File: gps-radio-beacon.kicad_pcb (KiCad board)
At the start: 2 copper layers, 106.4 x 69.7 mm, 34 parts, among them J1 Conn_01x16, J2 Conn_01x16, J3 Conn_Coaxial, J4 Conn_Coaxial, P1 USB_C_Plug_USB2.0, Q1 Q_PMOS_DGS, U1 PGA2040, U2 Si4463, U3 MAX-M10S, U4 NCP1117-3.3_SOT223

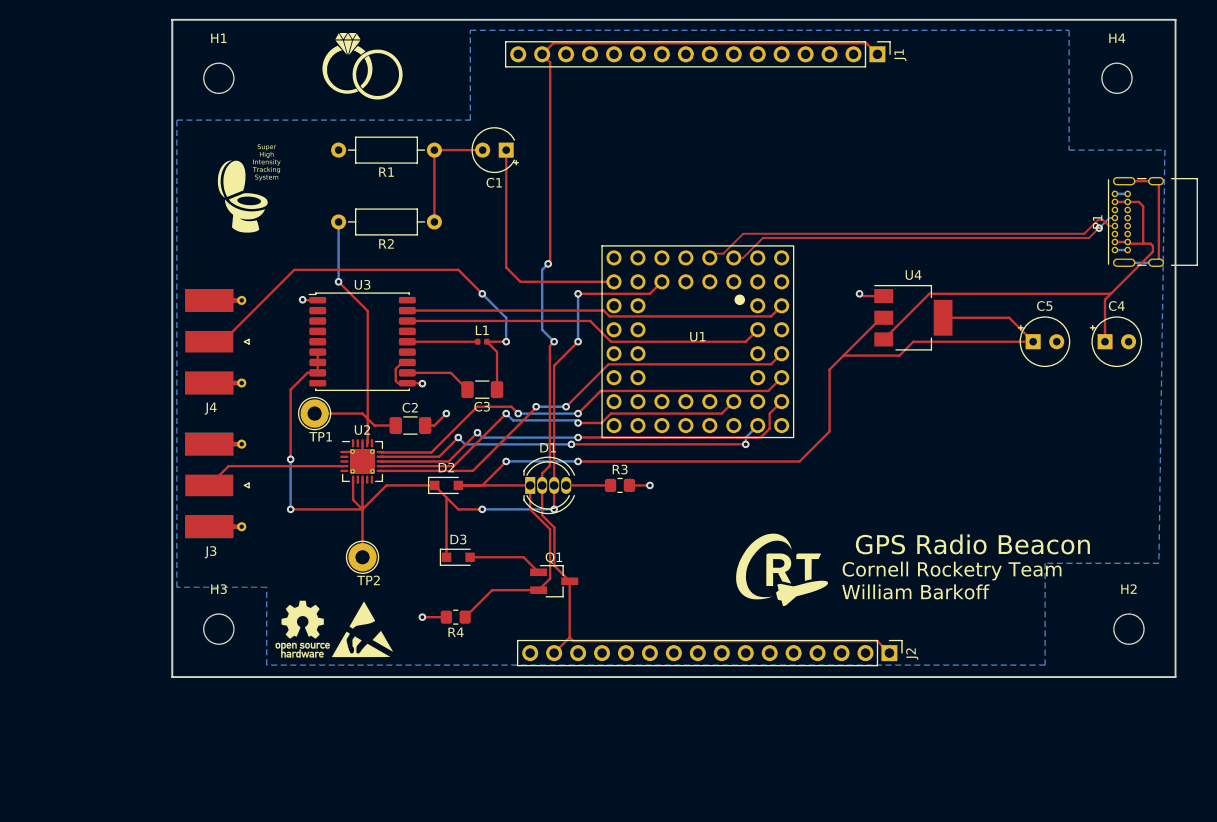
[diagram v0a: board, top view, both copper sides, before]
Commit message: redesign for use with RFM95
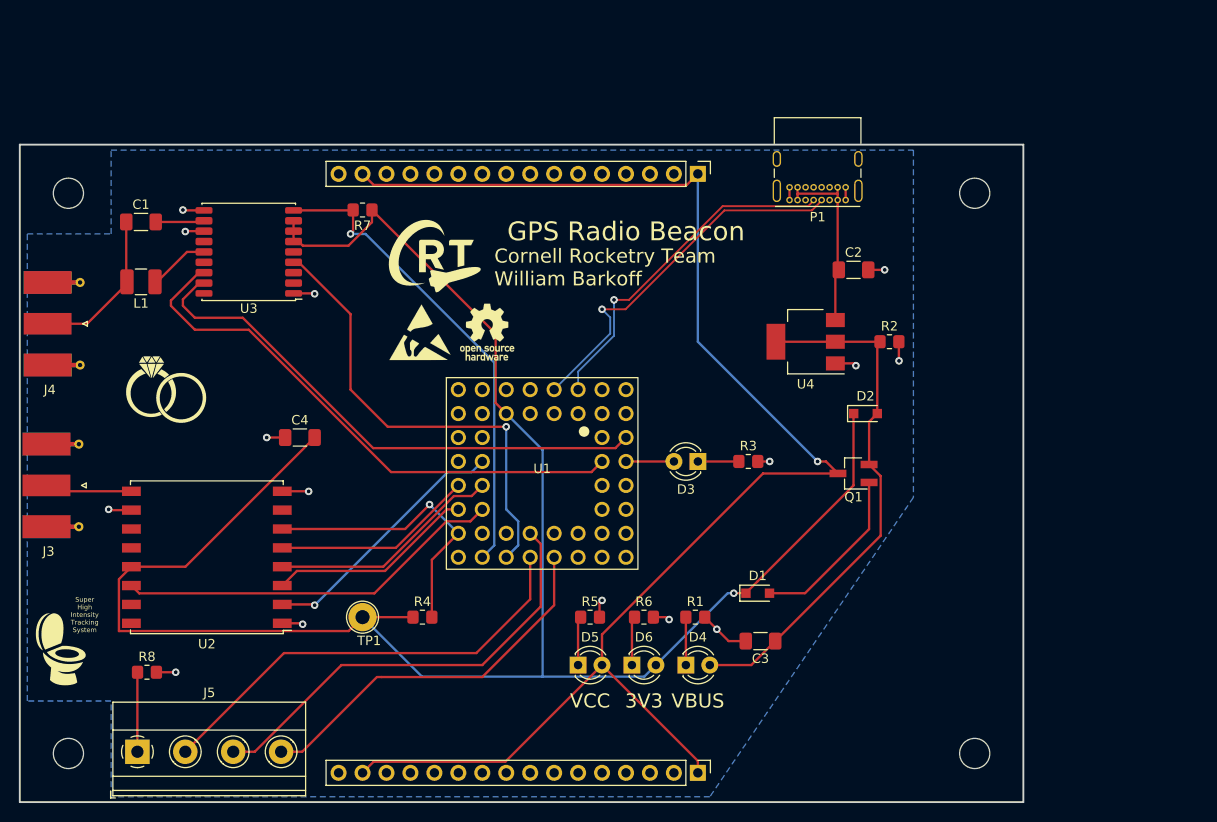
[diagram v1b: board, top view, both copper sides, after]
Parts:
- removed C5: 10u, Capacitor_THT:CP_Radial_Tantal_D5.0mm_P2.50mm
- removed TP2: TestPoint, TestPoint:TestPoint_Loop_D2.54mm_Drill1.5mm_Beaded
- added D4: LED, LED_THT:LED_D3.0mm, F.Cu at (153.7, 130.8)
- added D5: LED, LED_THT:LED_D3.0mm, F.Cu at (142.2, 130.8)
- added D6: LED, LED_THT:LED_D3.0mm, F.Cu at (147.9, 130.8)
- added J5: Screw_Terminal_01x04, TerminalBlock_Phoenix:TerminalBlock_Phoenix_MKDS-1,5-4-5.08_1x04_P5.08mm_Horizontal, F.Cu at (95.5, 140.0)
- added R5: 200, Resistor_SMD:R_0805_2012Metric_Pad1.20x1.40mm_HandSolder, F.Cu at (143.5, 125.7)
- added R6: 200, Resistor_SMD:R_0805_2012Metric_Pad1.20x1.40mm_HandSolder, F.Cu at (149.2, 125.7)
- added R7: 10k, Resistor_SMD:R_0805_2012Metric_Pad1.20x1.40mm_HandSolder, F.Cu at (119.4, 82.5)
- added R8: 200, Resistor_SMD:R_0805_2012Metric_Pad1.20x1.40mm_HandSolder, F.Cu at (96.5, 131.6)
- C1: value 100n -> 10n; footprint Capacitor_THT:CP_Radial_Tantal_D4.5mm_P2.50mm -> Capacitor_SMD:C_1206_3216Metric_Pad1.33x1.80mm_HandSolder
- C2: value 4.7n -> 10u
- C3: value 10n -> 10u
- C4: footprint Capacitor_THT:CP_Radial_Tantal_D5.0mm_P2.50mm -> Capacitor_SMD:C_1206_3216Metric_Pad1.33x1.80mm_HandSolder
- D1: value LED_RGBK -> D_Schottky; footprint LED_THT:LED_D5.0mm-4_RGB -> Diode_SMD:D_SOD-323_HandSoldering
- D3: value D_Schottky -> LED; footprint Diode_SMD:D_SOD-323_HandSoldering -> LED_THT:LED_D3.0mm
- L1: footprint Inductor_SMD:L_0402_1005Metric -> Inductor_SMD:L_1210_3225Metric_Pad1.42x2.65mm_HandSolder
- R1: value 4.7k -> 200; footprint Resistor_THT:R_Axial_DIN0207_L6.3mm_D2.5mm_P10.16mm_Horizontal -> Resistor_SMD:R_0805_2012Metric_Pad1.20x1.40mm_HandSolder
- R2: value 4.7k -> 10k; footprint Resistor_THT:R_Axial_DIN0207_L6.3mm_D2.5mm_P10.16mm_Horizontal -> Resistor_SMD:R_0805_2012Metric_Pad1.20x1.40mm_HandSolder
- U2: value Si4463 -> RFM95W-915S2; footprint Package_DFN_QFN:QFN-20-1EP_4x4mm_P0.5mm_EP2.6x2.6mm_ThermalVias -> RF_Module:HOPERF_RFM9XW_SMD
- moved C4 86.0 mm to (112.7, 106.7)
- moved H4 73.2 mm to (184.3, 140.2)
- moved R1 56.7 mm to (154.7, 125.7), turned to 0 degrees
- moved G*** 51.7 mm to (87.4, 129.3)
- moved R2 49.9 mm to (175.3, 96.5), turned to 0 degrees
- moved C2 49.8 mm to (171.4, 88.9)
- moved G*** 49.6 mm to (127.0, 87.4)
- moved H2 49.0 mm to (184.3, 80.8)
- moved D2 45.1 mm to (172.7, 104.1)
- moved G*** 40.1 mm to (98.6, 101.6)
- moved C3 39.8 mm to (161.6, 128.3)
- moved C1 39.5 mm to (95.9, 83.8), turned to 0 degrees
- moved REF** 37.1 mm to (132.6, 95.5)
- moved L1 36.7 mm to (95.9, 90.2), turned to 180 degrees
- moved Q1 33.7 mm to (171.4, 110.5), turned to 180 degrees
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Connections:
- C2 pad 1: /AFSK_SIGNAL -> +5V
- C2 pad 2: GND -> <NO NET>
- C3 pad 1: Net-(C3-Pad1) -> VBUS
- C3 pad 2: Net-(C3-Pad2) -> <NO NET>
- C4 pad 1: Net-(C4-Pad1) -> <NO NET>
- C4 pad 2: GND -> +3V3
- D1 pad 1: VBUS -> +3V3
- D1 pad 2: VCC -> Net-(D1-Pad2)
- D3 pad 1: +3V3 -> Net-(D3-Pad1)
- J1 pad 16: GND -> <NO NET>
- J1 pad 2: GND -> <NO NET>
- J2 pad 16: GND -> <NO NET>
- J2 pad 2: GND -> <NO NET>
- J3 pad 2: GND -> <NO NET>
- J4 pad 1: Net-(C3-Pad1) -> Net-(C1-Pad1)
- J4 pad 2: GND -> <NO NET>
- L1 pad 2: Net-(C3-Pad1) -> Net-(C1-Pad1)
- P1 pad A1: GND -> <NO NET>
- P1 pad A12: GND -> <NO NET>
- P1 pad A4: Net-(C4-Pad1) -> +5V
- P1 pad A9: Net-(C4-Pad1) -> +5V
- P1 pad B1: GND -> <NO NET>
- P1 pad B12: GND -> <NO NET>
- P1 pad B4: Net-(C4-Pad1) -> +5V
- P1 pad B9: Net-(C4-Pad1) -> +5V
- P1 pad S1: unconnected-(P1-PadS1) -> <NO NET>
- Q1 pad 1: Net-(D3-Pad2) -> Net-(D1-Pad2)
- R1 pad 1: Net-(C1-Pad2) -> Net-(D4-Pad1)
- R1 pad 2: GND -> <NO NET>
- R2 pad 1: Net-(C1-Pad2) -> VBUS
- R2 pad 2: /AFSK_SIGNAL -> <NO NET>
- R3 pad 1: Net-(D1-Pad4) -> Net-(D3-Pad1)
- R3 pad 2: GND -> <NO NET>
- R4 pad 1: VBUS -> +3V3
- R4 pad 2: GND -> /RADIO_RESET
- TP1 pad 1: /AFSK_SIGNAL -> +3V3
- U1 pad A1: GND -> <NO NET>
- U1 pad A3: GND -> <NO NET>
- U1 pad A8: GND -> <NO NET>
- U1 pad B1: Net-(C1-Pad1) -> unconnected-(U1-PadB1)
- U1 pad B2: GND -> <NO NET>
- U1 pad B7: GND -> <NO NET>
- U1 pad D2: unconnected-(U1-PadD2) -> /RADIO_MISO
- U1 pad D8: unconnected-(U1-PadD8) -> Net-(D3-Pad2)
- U1 pad E1: unconnected-(U1-PadE1) -> /RADIO_CS
- U1 pad E2: unconnected-(U1-PadE2) -> /RADIO_SCK
- U1 pad E8: /~{RADIO_INT} -> unconnected-(U1-PadE8)
- U1 pad F1: unconnected-(U1-PadF1) -> /RADIO_MOSI
- U1 pad F2: unconnected-(U1-PadF2) -> /RADIO_IRQ
- U1 pad F8: /~{RADIO_CS} -> unconnected-(U1-PadF8)
- U1 pad G1: unconnected-(U1-PadG1) -> /RADIO_RESET
- U1 pad G2: GND -> <NO NET>
- U1 pad G4: unconnected-(U1-PadG4) -> /IND_LED_2
- U1 pad G6: /RADIO_SCLK -> unconnected-(U1-PadG6)
- U1 pad G7: GND -> <NO NET>
- U1 pad G8: /RADIO_MISO -> unconnected-(U1-PadG8)
- U1 pad H1: GND -> <NO NET>
- U1 pad H2: unconnected-(U1-PadH2) -> /GPS_RESET
- U1 pad H3: unconnected-(U1-PadH3) -> /GPS_TIMEPULSE
- U1 pad H4: unconnected-(U1-PadH4) -> /IND_LED_1
- U1 pad H5: unconnected-(U1-PadH5) -> /IND_LED_3
- U1 pad H7: /RADIO_MOSI -> unconnected-(U1-PadH7)
- U1 pad H8: GND -> <NO NET>
- U2 pad 1: GND -> <NO NET>
- U2 pad 10: unconnected-(U2-Pad10) -> <NO NET>
- U2 pad 11: /~{RADIO_INT} -> unconnected-(U2-Pad11)
- U2 pad 12: /RADIO_SCLK -> unconnected-(U2-Pad12)
- U2 pad 13: /RADIO_MISO -> +3V3
- U2 pad 14: /RADIO_MOSI -> /RADIO_IRQ
- U2 pad 15: /~{RADIO_CS} -> unconnected-(U2-Pad15)
- U2 pad 2: unconnected-(U2-Pad2) -> /RADIO_MISO
- U2 pad 3: unconnected-(U2-Pad3) -> /RADIO_MOSI
- U2 pad 4: Net-(J3-Pad1) -> /RADIO_SCK
- U2 pad 5: unconnected-(U2-Pad5) -> /RADIO_CS
- U2 pad 6: +3V3 -> /RADIO_RESET
- U2 pad 8: +3V3 -> <NO NET>
- U2 pad 9: unconnected-(U2-Pad9) -> Net-(J3-Pad1)
- U3 pad 1: GND -> <NO NET>
- U3 pad 10: GND -> <NO NET>
- U3 pad 11: Net-(C3-Pad2) -> Net-(C1-Pad2)
- U3 pad 12: GND -> <NO NET>
- U3 pad 9: unconnected-(U3-Pad9) -> /GPS_RESET
- U4 pad 1: GND -> <NO NET>
- U4 pad 3: Net-(C4-Pad1) -> +5V
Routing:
- net +3V3: track 100.1 -> 205.0 mm, vias 6 -> 1
- net VBUS: track 116.5 -> 56.4 mm, vias 2 -> 0
- net /GPS_RESET: track 0.00 -> 51.0 mm, vias 0 -> 1
- net Net-(C4-Pad1): track 49.6 -> 0.00 mm
- net /GPS_TIMEPULSE: track 0.00 -> 49.4 mm, vias 0 -> 1
- net /~{RADIO_INT}: track 47.9 -> 0.00 mm, vias 2 -> 0
- net /IND_LED_1: track 0.00 -> 47.7 mm
- net /IND_LED_2: track 0.00 -> 47.2 mm
- net /~{RADIO_CS}: track 46.4 -> 0.00 mm, vias 2 -> 0
- net Net-(C3-Pad1): track 45.5 -> 0.00 mm, vias 2 -> 0
- net /RADIO_IRQ: track 0.00 -> 41.2 mm
- net /RADIO_SCLK: track 41.1 -> 0.00 mm, vias 2 -> 0
- net /IND_LED_3: track 0.00 -> 40.4 mm
- net <NO NET>: track 0.00 -> 37.1 mm, vias 0 -> 15
- net /AFSK_SIGNAL: track 32.6 -> 0.00 mm, vias 1 -> 0
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- added copper zone on B.Cu, net <NO NET>
- removed copper zone on B.Cu, net GND
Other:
- board text added: "3V3"
- board text added: "REV YYYY-MM-DD"
- board text added: "VBUS"
- board text added: "VCC"
- board text removed: "REV 2022-11-20"

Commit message: rearrange a few components
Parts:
- removed the G*** at (98.6, 101.6)
- moved G*** 52.6 mm to (166.6, 121.9)
- moved REF** 51.7 mm to (183.9, 88.9)
- moved G*** 46.3 mm to (98.6, 84.3)
- moved REF** 25.2 mm to (102.6, 106.2)
- moved C3 24.3 mm to (178.3, 110.7), turned to 0 degrees
- moved C4 24.2 mm to (114.3, 130.8)
- moved L1 10.8 mm to (95.2, 101.0)
- moved R7 10.8 mm to (118.7, 93.3)
- moved U3 10.8 mm to (106.7, 97.8)
- moved C1 10.8 mm to (96.0, 94.6)
- moved R1 8.39 mm to (146.3, 126.0)
- moved D4 8.38 mm to (145.3, 130.8)
- moved D6 8.00 mm to (139.9, 130.8)
- moved R6 7.99 mm to (141.2, 126.0)
- moved R5 7.89 mm to (135.6, 126.0)
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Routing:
- net +3V3: track 205.0 -> 169.7 mm
- net VCC: track 156.1 -> 170.6 mm, vias 1 -> 2
- net /GPS_TIMEPULSE: track 49.4 -> 40.8 mm
- net VBUS: track 56.4 -> 64.2 mm
- net /GPS_RESET: track 51.0 -> 47.4 mm
- net <NO NET>: track 37.1 -> 39.5 mm, vias 15 -> 16
- net Net-(D1-Pad2): track 18.3 -> 20.0 mm
- net /IND_LED_3: track 40.4 -> 39.0 mm
- net /IND_LED_2: track 47.2 -> 45.9 mm
- net Net-(C1-Pad1): track 16.9 -> 15.6 mm
- net /GPS_SCL: track 57.3 -> 56.0 mm
- net /IND_LED_1: track 47.7 -> 46.6 mm
- net Net-(C1-Pad2): track 5.17 -> 4.41 mm
- net /GPS_SDA: track 58.8 -> 59.4 mm
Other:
- board text added: "Alpha"
- board text added: "Beta"
- board text added: "GPS"
- board text added: "GPS Radio Beacon Cornell Rocketry William Barkoff Nov 28, 2022"
- board text added: "RF"
- board text removed: "Cornell Rocketry Team William Barkoff"
- board text removed: "GPS Radio Beacon"

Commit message: reroute some stuff
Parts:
- moved R7 1.81 mm to (117.3, 94.5), turned to 90 degrees
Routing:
- net +3V3: track 169.7 -> 166.5 mm
- net /GPS_RESET: track 47.4 -> 46.2 mm
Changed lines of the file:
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@@
   )
   (footprint "Resistor_SMD:R_0805_2012Metric_Pad1.20x1.40mm_HandSolder" (layer "F.Cu")
-    (at 118.745 93.345 180)
+    (at 117.348 94.488 90)
     (descr "Resistor SMD 0805 (2012 Metric), square (rectangular) end terminal, IPC_7351 nominal with elongated pad for handsoldering. (Body size source: IPC-SM-782 page 72, https://www.pcb-3d.com/wordpress/wp-content/uploads/ipc-sm-782a_amendment_1_and_2.pdf), generated with kicad-footprint-generator")
     (tags "resistor handsolder")
@@
     (property "Sheetname" "")
     (attr smd)
-    (fp_text reference "R7" (at 0 -1.65) (layer "F.SilkS")
+    (fp_text reference "R7" (at 2.54 0 180) (layer "F.SilkS")
       (effects (font (size 1 1) (thickness 0.15)))
     )
-    (fp_text value "10k" (at 0 1.65) (layer "F.Fab")
+    (fp_text value "10k" (at 0 1.65 90) (layer "F.Fab")
       (effects (font (size 1 1) (thickness 0.15)))
     )
-    (fp_text user "${REFERENCE}" (at 0 0) (layer "F.Fab")
+    (fp_text user "${REFERENCE}" (at 0 0 90) (layer "F.Fab")
       (effects (font (size 0.5 0.5) (thickness 0.08)))
     )
@@
     (fp_line (start 1 -0.625) (end 1 0.625) (layer "F.Fab") (width 0.1))
     (fp_line (start -1 -0.625) (end 1 -0.625) (layer "F.Fab") (width 0.1))
-    (pad "1" smd roundrect (at -1 0 180) (size 1.2 1.4) (layers "F.Cu" "F.Paste" "F.Mask") (roundrect_rratio 0.208333)
+    (pad "1" smd roundrect (at -1 0 90) (size 1.2 1.4) (layers "F.Cu" "F.Paste" "F.Mask") (roundrect_rratio 0.208333)
       (net 5 "+3V3") (pintype "passive"))
-    (pad "2" smd roundrect (at 1 0 180) (size 1.2 1.4) (layers "F.Cu" "F.Paste" "F.Mask") (roundrect_rratio 0.208333)
+    (pad "2" smd roundrect (at 1 0 90) (size 1.2 1.4) (layers "F.Cu" "F.Paste" "F.Mask") (roundrect_rratio 0.208333)
       (net 48 "/GPS_RESET") (pintype "passive"))
     (model "${KICAD6_3DMODEL_DIR}/Resistor_SMD.3dshapes/R_0805_2012Metric.wrl"
@@
   (segment (start 117.251536 97.133769) (end 112.416231 97.133769) (width 0.25) (layer "F.Cu") (net 5))
   (segment (start 115.775 130.7225) (end 115.775 127.205) (width 0.25) (layer "F.Cu") (net 5))
+  (segment (start 117.348 95.488) (end 117.348 97.037305) (width 0.25) (layer "F.Cu") (net 5))
   (segment (start 119.38 125.73) (end 124.73 125.73) (width 0.25) (layer "F.Cu") (net 5))
   (segment (start 111.43 95.59) (end 111.43 94.49) (width 0.25) (layer "F.Cu") (net 5))
@@
   (segment (start 143.764 124.968) (end 143.764 129.535) (width 0.25) (layer "F.Cu") (net 5))
   (segment (start 154.8384 118.872) (end 153.69 118.872) (width 0.25) (layer "F.Cu") (net 5))
+  (segment (start 117.348 97.037305) (end 117.251536 97.133769) (width 0.25) (layer "F.Cu") (net 5))
   (segment (start 115.775 127.205) (end 117.905 127.205) (width 0.25) (layer "F.Cu") (net 5))
-  (segment (start 119.745 94.640305) (end 117.251536 97.133769) (width 0.25) (layer "F.Cu") (net 5))
   (segment (start 117.905 127.205) (end 119.38 125.73) (width 0.25) (layer "F.Cu") (net 5))
   (segment (start 93.545 127.205) (end 115.775 127.205) (width 0.25) (layer "F.Cu") (net 5))
@@
   (segment (start 115.8625 130.81) (end 115.775 130.7225) (width 0.25) (layer "F.Cu") (net 5))
   (segment (start 93.545 121.705) (end 93.545 127.205) (width 0.25) (layer "F.Cu") (net 5))
-  (segment (start 119.745 93.345) (end 119.745 94.640305) (width 0.25) (layer "F.Cu") (net 5))
   (segment (start 149.86 118.872) (end 143.764 124.968) (width 0.25) (layer "F.Cu") (net 5))
   (segment (start 111.972462 96.69) (end 111.43 96.69) (width 0.25) (layer "F.Cu") (net 5))
@@
   (via (at 126.4877 113.7877) (size 0.8) (drill 0.4) (layers "F.Cu" "B.Cu") (net 47))
   (segment (start 126.4877 113.7877) (end 129.54 116.84) (width 0.25) (layer "B.Cu") (net 47))
-  (segment (start 114.89 93.39) (end 117.7 93.39) (width 0.25) (layer "F.Cu") (net 48))
-  (segment (start 111.43 93.39) (end 114.89 93.39) (width 0.25) (layer "F.Cu") (net 48))
-  (segment (start 117.348 93.742) (end 117.745 93.345) (width 0.25) (layer "F.Cu") (net 48))
-  (segment (start 115.234 93.39) (end 115.316 93.472) (width 0.25) (layer "F.Cu") (net 48))
-  (segment (start 114.89 93.39) (end 115.234 93.39) (width 0.25) (layer "F.Cu") (net 48))
-  (segment (start 117.7 93.39) (end 117.745 93.345) (width 0.25) (layer "F.Cu") (net 48))
-  (segment (start 117.348 94.996) (end 117.348 93.742) (width 0.25) (layer "F.Cu") (net 48))
-  (via (at 117.348 94.996) (size 0.8) (drill 0.4) (layers "F.Cu" "B.Cu") (net 48))
-  (segment (start 133.35 98.806) (end 133.35 118.11) (width 0.25) (layer "B.Cu") (net 48))
-  (segment (start 129.54 94.996) (end 133.35 98.806) (width 0.25) (layer "B.Cu") (net 48))
-  (segment (start 133.35 118.11) (end 132.08 119.38) (width 0.25) (layer "B.Cu") (net 48))
-  (segment (start 117.348 94.996) (end 129.54 94.996) (width 0.25) (layer "B.Cu") (net 48))
-  (segment (start 133.35 98.739009) (end 133.35 98.806) (width 0.25) (layer "B.Cu") (net 48))
+  (segment (start 117.348 93.488) (end 111.528 93.488) (width 0.25) (layer "F.Cu") (net 48))
+  (segment (start 111.528 93.488) (end 111.43 93.39) (width 0.25) (layer "F.Cu") (net 48))
+  (segment (start 117.364 93.472) (end 117.348 93.488) (width 0.25) (layer "F.Cu") (net 48))
+  (segment (start 119.38 93.472) (end 117.364 93.472) (width 0.25) (layer "F.Cu") (net 48))
+  (via (at 119.38 93.472) (size 0.8) (drill 0.4) (layers "F.Cu" "B.Cu") (net 48))
+  (segment (start 133.096 100.076) (end 132.588 99.568) (width 0.25) (layer "B.Cu") (net 48))
+  (segment (start 132.588 99.568) (end 122.428 99.568) (width 0.25) (layer "B.Cu") (net 48))
+  (segment (start 132.08 119.38) (end 133.35 118.11) (width 0.25) (layer "B.Cu") (net 48))
+  (segment (start 133.35 118.11) (end 133.096 117.856) (width 0.25) (layer "B.Cu") (net 48))
+  (segment (start 122.428 99.568) (end 119.38 96.52) (width 0.25) (layer "B.Cu") (net 48))
+  (segment (start 133.096 117.856) (end 133.096 100.076) (width 0.25) (layer "B.Cu") (net 48))
+  (segment (start 119.38 96.52) (end 119.38 93.472) (width 0.25) (layer "B.Cu") (net 48))
   (segment (start 99.568 106.172) (end 99.568 101.6) (width 0.25) (layer "F.Cu") (net 60))
   (segment (start 147.32 106.68) (end 146.195 107.805) (width 0.25) (layer "F.Cu") (net 60))

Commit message: Add license
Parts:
- added G***: LOGO, grb:coffee, F.Cu at (132.6, 90.4)
- REF**: value OSHW-Logo_5.7x6mm_SilkScreen -> OSHW-Symbol_6.7x6mm_SilkScreen; footprint Symbol:OSHW-Logo_5.7x6mm_SilkScreen -> Symbol:OSHW-Symbol_6.7x6mm_SilkScreen; moved to B.Cu
- moved REF** 39.7 mm to (181.9, 128.5), turned to 180 degrees
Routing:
- net (no net): track 0.00 -> 11.2 mm
- net /GPS_SDA: track 59.4 -> 58.8 mm
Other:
- board text added: "Gimme!"
- board text added: "Open source hardware!"
- board text added: "REV ${ISSUE_DATE}"
- board text added: "https://g.cornellrocketryteam.com/oshw Licensed under CERN-OHL-W v2"
- board text removed: "REV YYYY-MM-DD"

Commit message: final updates!
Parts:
- added JP1: SolderJumper_2_Bridged, Jumper:SolderJumper-2_P1.3mm_Bridged_RoundedPad1.0x1.5mm, F.Cu at (176.3, 78.7)
- moved G*** 8.19 mm to (124.5, 91.4)
- moved J1 1.39 mm to (155.3, 80.1)
- moved J2 1.39 mm to (155.3, 140.9)
- moved REF** 1.15 mm to (181.7, 127.4)
- moved REF** 0.72 mm to (102.1, 106.7)
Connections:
- P1 pad B6: (no net) -> /PWR-USB/USB_D+
- P1 pad B7: (no net) -> /PWR-USB/USB_D-
- P1 pad S1: <NO NET> -> Net-(P1-PadS1)
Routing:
- net Net-(P1-PadS1): track 0.00 -> 20.8 mm
- net (no net): track 11.2 -> 0.00 mm
- net <NO NET>: track 39.5 -> 41.9 mm, vias 16 -> 17
- net VCC: track 170.6 -> 168.6 mm, vias 2 -> 1
- net /PWR-USB/USB_D-: track 36.8 -> 38.5 mm
- net /PWR-USB/USB_D+: track 39.5 -> 41.2 mm
- net /GPS_TIMEPULSE: track 40.8 -> 40.2 mm
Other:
- board text added: "GND"
- board text added: "GPS Radio Beacon Cornell Rocketry William Barkoff ${ISSUE_DATE}"
- board text added: "Issue Date ${ISSUE_DATE} Revision ${REVISION}"
- board text removed: "GPS Radio Beacon Cornell Rocketry William Barkoff Nov 28, 2022"
- board text removed: "REV ${ISSUE_DATE}"

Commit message: Add BOOTSEL button
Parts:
- added SW1: SW_Push, Button_Switch_THT:SW_PUSH_6mm, F.Cu at (134.5, 88.6)
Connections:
- P1 pad B6: /PWR-USB/USB_D+ -> (no net)
- P1 pad B7: /PWR-USB/USB_D- -> (no net)
- U1 pad A7: unconnected-(U1-PadA7) -> Net-(SW1-Pad2)
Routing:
- net Net-(SW1-Pad2): track 0.00 -> 17.2 mm
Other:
- board text added: "BOOTSEL"
